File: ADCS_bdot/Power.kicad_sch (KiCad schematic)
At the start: 4 parts, among them U3 TPSM861253RDXR, U4 TLV77325PDQNR

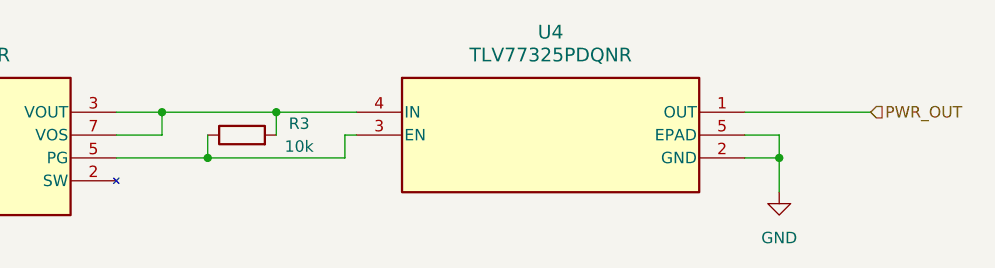
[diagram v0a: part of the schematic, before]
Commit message: feat: Gyro and Mag RC Filter
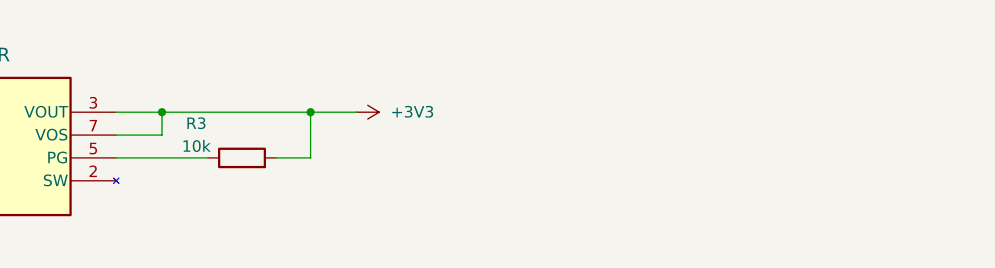
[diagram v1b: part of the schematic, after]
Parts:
- removed U4: TLV77325PDQNR, Footprintlib_adcs_bdot:X2SON_DQN4_TEX, symbol Symbollib_adcs_bdot:TLV77325PDQNR
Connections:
- net +3V3: now reaches R3.2, U3.3 (VOUT), U3.7 (VOS)
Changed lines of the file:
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@@
 	(paper "A4")
+	(junction
+		(at 144.78 91.44)
+		(diameter 0)
+		(color 0 0 0 0)
+	)
 	(junction
 		(at 82.55 91.44)
@@
 	)
 	(junction
-		(at 149.86 96.52)
+		(at 161.29 91.44)
 		(diameter 0)
 		(color 0 0 0 0)
 	)
-	(junction
-		(at 157.48 91.44)
-		(diameter 0)
-		(color 0 0 0 0)
-	)
-	(junction
-		(at 144.78 91.44)
-		(diameter 0)
-		(color 0 0 0 0)
-	)
-	(junction
-		(at 213.36 96.52)
-		(diameter 0)
-		(color 0 0 0 0)
-	)
 	(wire
 		(pts
@@
 	(wire
 		(pts
-			(xy 157.48 91.44) (xy 157.48 93.98)
-		)
-		(stroke
-			(width 0)
-			(type default)
-		)
-	)
-	(wire
-		(pts
-			(xy 209.55 91.44) (xy 223.52 91.44)
-		)
-		(stroke
-			(width 0)
-			(type default)
-		)
-	)
-	(wire
-		(pts
-			(xy 144.78 91.44) (xy 157.48 91.44)
-		)
-		(stroke
-			(width 0)
-			(type default)
-		)
-	)
-	(wire
-		(pts
-			(xy 157.48 91.44) (xy 166.37 91.44)
+			(xy 161.29 96.52) (xy 161.29 91.44)
+		)
+		(stroke
+			(width 0)
+			(type default)
+		)
+	)
+	(wire
+		(pts
+			(xy 161.29 91.44) (xy 166.37 91.44)
+		)
+		(stroke
+			(width 0)
+			(type default)
+		)
+	)
+	(wire
+		(pts
+			(xy 144.78 91.44) (xy 161.29 91.44)
 		)
 		(stroke
@@
 	(wire
 		(pts
-			(xy 213.36 96.52) (xy 213.36 100.33)
-		)
-		(stroke
-			(width 0)
-			(type default)
-		)
-	)
-	(wire
-		(pts
-			(xy 213.36 93.98) (xy 213.36 96.52)
-		)
-		(stroke
-			(width 0)
-			(type default)
-		)
-	)
-	(wire
-		(pts
 			(xy 92.71 93.98) (xy 96.52 93.98)
 		)
@@
 	(wire
 		(pts
-			(xy 209.55 96.52) (xy 213.36 96.52)
-		)
-		(stroke
-			(width 0)
-			(type default)
-		)
-	)
-	(wire
-		(pts
-			(xy 209.55 93.98) (xy 213.36 93.98)
-		)
-		(stroke
-			(width 0)
-			(type default)
-		)
-	)
-	(wire
-		(pts
 			(xy 92.71 96.52) (xy 96.52 96.52)
 		)
@@
 	(wire
 		(pts
-			(xy 165.1 96.52) (xy 149.86 96.52)
-		)
-		(stroke
-			(width 0)
-			(type default)
-		)
-	)
-	(wire
-		(pts
 			(xy 139.7 91.44) (xy 144.78 91.44)
 		)
@@
 	(wire
 		(pts
+			(xy 157.48 96.52) (xy 161.29 96.52)
+		)
+		(stroke
+			(width 0)
+			(type default)
+		)
+	)
+	(wire
+		(pts
 			(xy 82.55 93.98) (xy 82.55 91.44)
 		)
@@
 	(wire
 		(pts
-			(xy 166.37 93.98) (xy 165.1 93.98)
-		)
-		(stroke
-			(width 0)
-			(type default)
-		)
-	)
-	(wire
-		(pts
 			(xy 82.55 91.44) (xy 96.52 91.44)
 		)
@@
 		(pts
 			(xy 92.71 100.33) (xy 92.71 96.52)
-		)
-		(stroke
-			(width 0)
-			(type default)
-		)
-	)
-	(wire
-		(pts
-			(xy 165.1 93.98) (xy 165.1 96.52)
-		)
-		(stroke
-			(width 0)
-			(type default)
-		)
-	)
-	(wire
-		(pts
-			(xy 149.86 96.52) (xy 149.86 93.98)
 		)
 		(stroke
@@
 		)
 	)
-	(hierarchical_label "PWR_OUT"
-		(shape input)
-		(at 223.52 91.44 0)
-		(effects
-			(font
-				(size 1.27 1.27)
-			)
-			(justify left)
-		)
-	)
 	(symbol
-		(lib_id "Symbollib_adcs_bdot:TLV77325PDQNR")
-		(at 166.37 91.44 0)
+		(lib_id "power:+3V3")
+		(at 166.37 91.44 270)
 		(unit 1)
 		(exclude_from_sim no)
@@
 		(dnp no)
 		(fields_autoplaced yes)
-		(property "Reference" "U4"
-			(at 187.96 82.55 0)
-			(effects
-				(font
-					(size 1.524 1.524)
-				)
-			)
-		)
-		(property "Value" "TLV77325PDQNR"
-			(at 187.96 85.09 0)
-			(effects
-				(font
-					(size 1.524 1.524)
-				)
-			)
-		)
-		(property "Footprint" "Footprintlib_adcs_bdot:X2SON_DQN4_TEX"
-			(at 182.88 86.36 0)
-			(effects
-				(font
-					(size 1.27 1.27)
-					(italic yes)
-				)
-				(hide yes)
-			)
-		)
-		(property "Datasheet" "https://www.ti.com/lit/gpn/tlv773"
-			(at 182.88 86.36 0)
-			(effects
-				(font
-					(size 1.27 1.27)
-					(italic yes)
-				)
-				(hide yes)
-			)
-		)
-		(property "Description" ""
+		(property "Reference" "#PWR019"
+			(at 162.56 91.44 0)
+			(effects
+				(font
+					(size 1.27 1.27)
+				)
+				(hide yes)
+			)
+		)
+		(property "Value" "+3V3"
+			(at 170.18 91.4399 90)
+			(effects
+				(font
+					(size 1.27 1.27)
+				)
+				(justify left)
+			)
+		)
+		(property "Footprint" ""
 			(at 166.37 91.44 0)
 			(effects
@@
 			)
 		)
-		(pin "4"
-		)
-		(pin "5"
-		)
-		(pin "2"
+		(property "Datasheet" ""
+			(at 166.37 91.44 0)
+			(effects
+				(font
+					(size 1.27 1.27)
+				)
+				(hide yes)
+			)
+		)
+		(property "Description" "Power symbol creates a global label with name \"+3V3\""
+			(at 166.37 91.44 0)
+			(effects
+				(font
+					(size 1.27 1.27)
+				)
+				(hide yes)
+			)
 		)
 		(pin "1"
 		)
-		(pin "3"
-		)
 		(instances
-			(project ""
+			(project "ADCS_bdot"
 				(path "/9a605480-5564-4a0e-ba7b-19a361378337/09105f10-a949-43fe-bd4d-bca407919f43"
-					(reference "U4")
+					(reference "#PWR019")
 					(unit 1)
 				)
@@
 	)
 	(symbol
-		(lib_id "power:GND")
-		(at 213.36 100.33 0)
-		(unit 1)
-		(exclude_from_sim no)
-		(in_bom yes)
-		(on_board yes)
-		(dnp no)
-		(fields_autoplaced yes)
-		(property "Reference" "#PWR019"
-			(at 213.36 106.68 0)
-			(effects
-				(font
-					(size 1.27 1.27)
-				)
-				(hide yes)
-			)
-		)
-		(property "Value" "GND"
-			(at 213.36 105.41 0)
-			(effects
-				(font
-					(size 1.27 1.27)
-				)
-			)
-		)
-		(property "Footprint" ""
-			(at 213.36 100.33 0)
-			(effects
-				(font
-					(size 1.27 1.27)
-				)
-				(hide yes)
-			)
-		)
-		(property "Datasheet" ""
-			(at 213.36 100.33 0)
-			(effects
-				(font
-					(size 1.27 1.27)
-				)
-				(hide yes)
-			)
-		)
-		(property "Description" "Power symbol creates a global label with name \"GND\" , ground"
-			(at 213.36 100.33 0)
-			(effects
-				(font
-					(size 1.27 1.27)
-				)
-				(hide yes)
-			)
-		)
-		(pin "1"
-		)
-		(instances
-			(project "ADCS_bdot"
-				(path "/9a605480-5564-4a0e-ba7b-19a361378337/09105f10-a949-43fe-bd4d-bca407919f43"
-					(reference "#PWR019")
-					(unit 1)
-				)
-			)
-		)
-	)
-	(symbol
 		(lib_id "Device:R")
-		(at 153.67 93.98 90)
+		(at 153.67 96.52 90)
 		(unit 1)
 		(exclude_from_sim no)
@@
 		(dnp no)
 		(property "Reference" "R3"
-			(at 160.02 92.71 90)
+			(at 148.59 92.71 90)
 			(effects
 				(font
@@
 		)
 		(property "Value" "10k"
-			(at 160.02 95.25 90)
+			(at 148.59 95.25 90)
 			(effects
 				(font
@@
 		)
 		(property "Footprint" ""
-			(at 153.67 95.758 90)
+			(at 153.67 98.298 90)
 			(effects
 				(font
@@
 		)
 		(property "Datasheet" "~"
-			(at 153.67 93.98 0)
+			(at 153.67 96.52 0)
 			(effects
 				(font
@@
 		)
 		(property "Description" "Resistor"
-			(at 153.67 93.98 0)
+			(at 153.67 96.52 0)
 			(effects
 				(font
@@
 		)
 		(instances
-			(project ""
+			(project "ADCS_bdot"
 				(path "/9a605480-5564-4a0e-ba7b-19a361378337/09105f10-a949-43fe-bd4d-bca407919f43"
 					(reference "R3")

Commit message: add: a bunch of stuff
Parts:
- removed R4: 10k, symbol Device:R
- added C10: 10u, Capacitor_SMD:C_0603_1608Metric_Pad1.08x0.95mm_HandSolder, symbol Device:C
- added C8: 22u, Capacitor_SMD:C_0603_1608Metric_Pad1.08x0.95mm_HandSolder, symbol Device:C
- added R8: 261k, Resistor_SMD:R_0603_1608Metric_Pad0.98x0.95mm_HandSolder, symbol Device:R
- added R9: 100k, Resistor_SMD:R_0603_1608Metric_Pad0.98x0.95mm_HandSolder, symbol Device:R
- R3: footprint (none) -> Resistor_SMD:R_0603_1608Metric_Pad0.98x0.95mm_HandSolder
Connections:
- net +3V3: now also C8.1
- net GND: now also C10.2, C8.2, R9.2
- net PWR_IN: now also C10.1, R8.1
- net at U3.6 (EN): now also R8.2, R9.1
